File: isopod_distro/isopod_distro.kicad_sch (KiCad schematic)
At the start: 57 parts, among them J1 CHG_IN, J10 IN, J11 IN, J12 IN, J13 IN, J14 IN, J15 IN, J16 BATT, J17 OUT, J18 OUT, J19 OUT, J2 OUT, J20 OUT, J21 OUT, J22 OUT, J23 IN, J24 IN, J25 IN, J26 IN, J27 IN, J28 IN, J29 BAL, J3 OUT, J30 Raspberry_Pi_2_3, J4 OUT, J5 OUT, J6 OUT, J7 OUT, J8 TO_DCDC, J9 FROM_DCDC, Q1 IRLR6225TRPBF, Q2 BSS138, Q3 BSS138, U1 MAX17205, U2 UPU-MAX-M8C, U3 adafruit_tdk_icm-20948

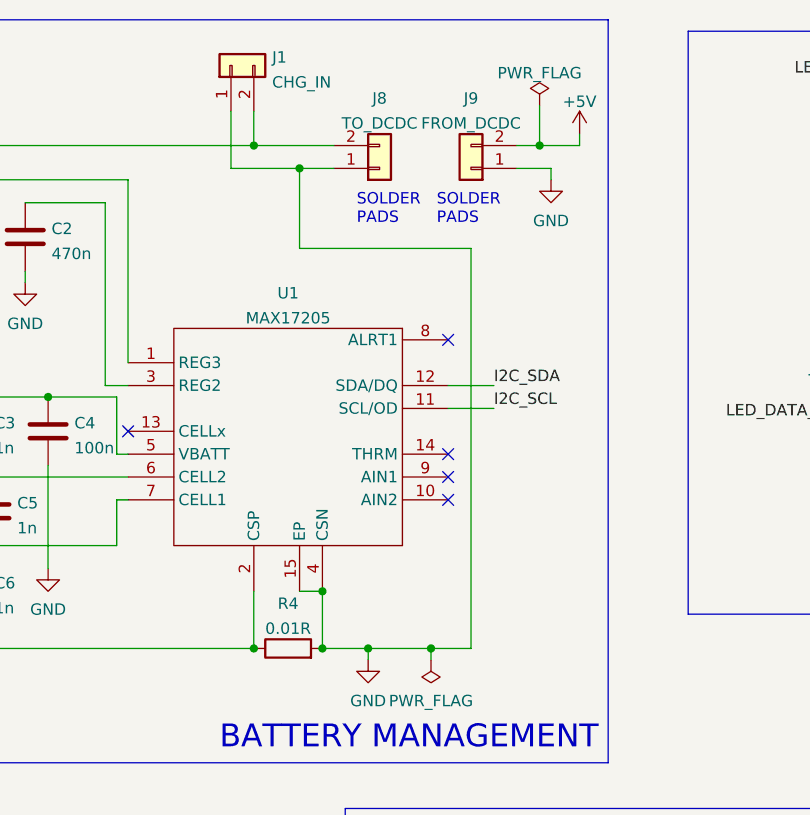
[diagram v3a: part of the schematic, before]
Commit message: Swap out batt/charge and DC-DC connectors
Use XT30 for battery and charge connectors and MOLEX mini-fit jr 4-way
for the DC-DC converter connection
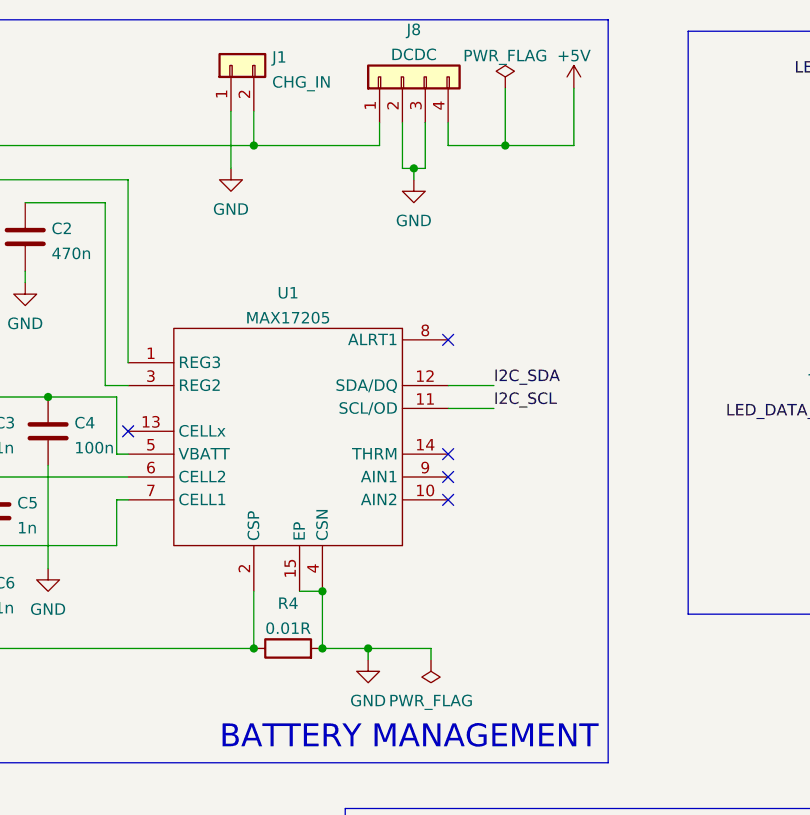
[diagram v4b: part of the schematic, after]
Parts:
- removed J8: TO_DCDC, TestPoint:TestPoint_2Pads_Pitch5.08mm_Drill1.3mm, symbol Connector_Generic:Conn_01x02
- removed J9: FROM_DCDC, TestPoint:TestPoint_2Pads_Pitch5.08mm_Drill1.3mm, symbol Connector_Generic:Conn_01x02
- added J8: DCDC, Connector_Molex:Molex_Mini-Fit_Jr_5566-04A_2x02_P4.20mm_Vertical, symbol Connector_Generic:Conn_01x04
- J1: footprint TestPoint:TestPoint_2Pads_Pitch5.08mm_Drill1.3mm -> Connector_AMASS:AMASS_XT30U-M_1x02_P5.0mm_Vertical
- J16: footprint Connector_AMASS:AMASS_XT60-M_1x02_P7.20mm_Vertical -> Connector_AMASS:AMASS_XT30U-M_1x02_P5.0mm_Vertical
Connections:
- net +5V: now also J8.4 (Pin_4)
- net GND: now also J8.2 (Pin_2), J8.3 (Pin_3)
- net at J1.2 (Pin_2), J16.2 (Pin_2), R1.1: now also J8.1 (Pin_1)
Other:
- note removed: "SOLDER PADS"

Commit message: Final schematic checks
* Add some DNF resistors for the fuel cell in case its temperature
  sensing can't be disabled
* Add some series resistors on I2C because the appnote says so
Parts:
- added R13, R14, R15, R16: DNF, Resistor_SMD:R_0603_1608Metric_Pad0.98x0.95mm_HandSolder, symbol Device:R
- added R7, R8: 150, Resistor_SMD:R_0603_1608Metric_Pad0.98x0.95mm_HandSolder, symbol Device:R
- Q1: Farnell (none) -> 2726021
- U1: Farnell (none) -> 3404585
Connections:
- net GND: now also R15.2, R16.2
- net I2C_SCL: now also R8.1; no longer U1.11 (SCL/OD)
- net I2C_SDA: now also R7.2; no longer U1.12 (SDA/DQ)
- net at R2.1: now also J29.2 (Pin_2); no longer J29.3 (Pin_3)
- net at U1.10 (AIN2): now also R14.2, R16.1
- net at U1.14 (THRM): now also R13.1, R14.1
- net at U1.9 (AIN1): now also R13.2, R15.1
- net at R3.1: now also J29.3 (Pin_3); no longer J29.2 (Pin_2)
- new net: R8.2, U1.11 (SCL/OD)
- new net: R7.1, U1.12 (SDA/DQ)
- no-connect marks 38 -> 35
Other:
- moved on the sheet: J29

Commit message: PCB silkscreen
Make the PCB silkscreen look neat: Remove most component references, add
a few values where appropriate, label connectors and pinouts, board name
etc.
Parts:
- J10: value IN -> IN 1
- J11: value IN -> IN 2
- J12: value IN -> IN 3
- J13: value IN -> IN 4
- J14: value IN -> IN 5
- J15: value IN -> IN 6
- J17: value OUT -> OUT 7
- J18: value OUT -> OUT 8
- J19: value OUT -> OUT 9
- J2: value OUT -> OUT 1
- J20: value OUT -> OUT 10
- J21: value OUT -> OUT 11
- J22: value OUT -> OUT 12
- J23: value IN -> IN 7
- J24: value IN -> IN 8
- J25: value IN -> IN 9
- J26: value IN -> IN 10
- J27: value IN -> IN 11
- J28: value IN -> IN 12
- J3: value OUT -> OUT 2
- J4: value OUT -> OUT 3
- J5: value OUT -> OUT 4
- J6: value OUT -> OUT 5
- J7: value OUT -> OUT 6
